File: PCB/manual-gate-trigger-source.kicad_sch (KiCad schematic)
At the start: 52 parts

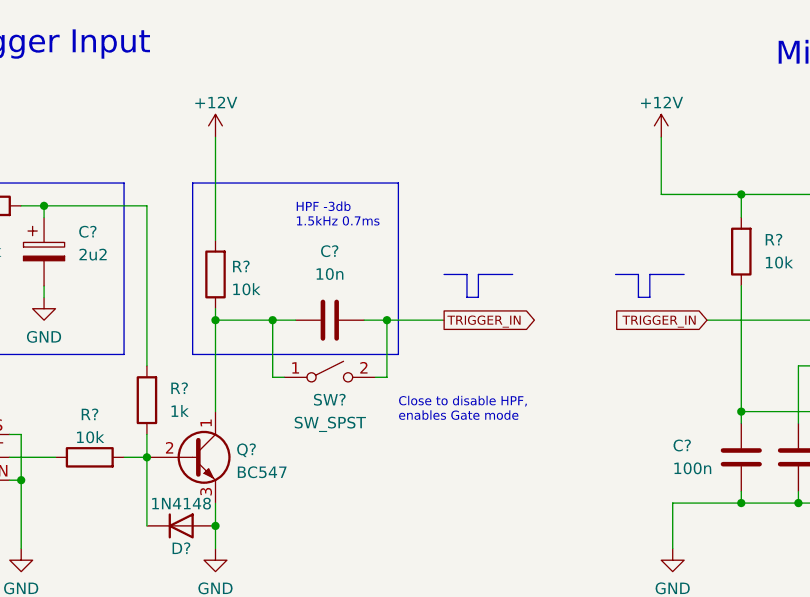
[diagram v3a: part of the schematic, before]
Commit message: :pencil2: Fix HPF for 555 input
As the signal is one-sided to V+, a second resistor was necessary.
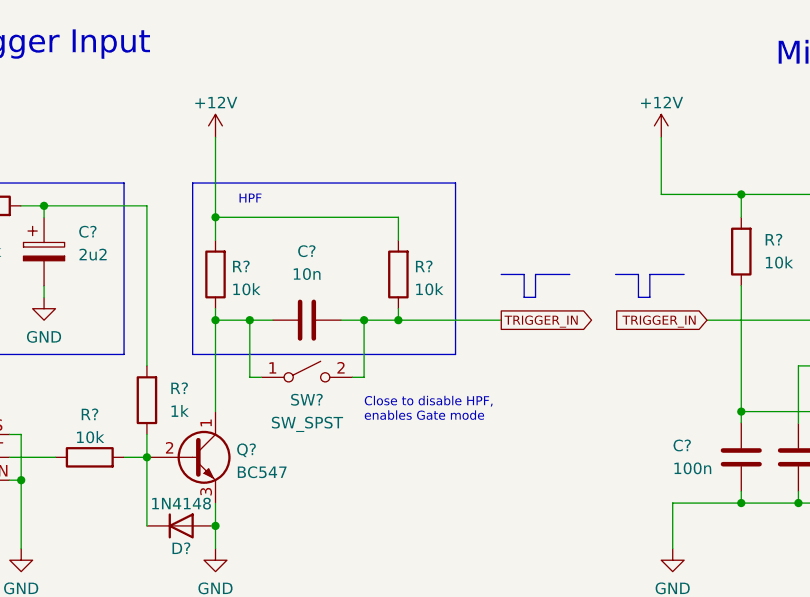
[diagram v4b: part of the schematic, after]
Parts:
- added R?: 10k, symbol Device:R
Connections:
- net +12V: now also R?.2
- net TRIGGER_IN: now also R?.1
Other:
- note added: "HPF"
- note removed: "HPF -3db 1.5kHz 0.7ms"
- moved on the sheet: C?, SW?
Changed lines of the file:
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@@
   (junction (at 102.87 157.48) (diameter 0) (color 0 0 0 0)
   )
-  (junction (at 80.01 58.42) (diameter 0) (color 0 0 0 0)
+  (junction (at 77.47 58.42) (diameter 0) (color 0 0 0 0)
   )
   (junction (at 198.12 138.43) (diameter 0) (color 0 0 0 0)
@@
   (junction (at 250.19 76.2) (diameter 0) (color 0 0 0 0)
   )
-  (junction (at 92.71 58.42) (diameter 0) (color 0 0 0 0)
+  (junction (at 93.98 58.42) (diameter 0) (color 0 0 0 0)
+  )
+  (junction (at 90.17 58.42) (diameter 0) (color 0 0 0 0)
   )
   (junction (at 73.66 81.28) (diameter 0) (color 0 0 0 0)
@@
   )
   (junction (at 232.41 130.81) (diameter 0) (color 0 0 0 0)
+  )
+  (junction (at 73.66 46.99) (diameter 0) (color 0 0 0 0)
   )
   (junction (at 247.65 146.05) (diameter 0) (color 0 0 0 0)
@@
   (no_connect (at 264.16 81.28))
   (no_connect (at 264.16 71.12))
-  (polyline (pts (xy 102.87 55.88) (xy 102.87 53.34))
+  (polyline (pts (xy 109.22 55.88) (xy 109.22 53.34))
     (stroke (width 0) (type solid) (color 0 0 0 0))
   )
@@
     (stroke (width 0) (type default) (color 0 0 0 0))
   )
-  (polyline (pts (xy 101.6 55.88) (xy 102.87 55.88))
+  (polyline (pts (xy 107.95 55.88) (xy 109.22 55.88))
     (stroke (width 0) (type solid) (color 0 0 0 0))
   )
@@
     (stroke (width 0) (type solid) (color 0 0 0 0))
   )
-  (wire (pts (xy 90.17 58.42) (xy 92.71 58.42))
+  (wire (pts (xy 87.63 58.42) (xy 90.17 58.42))
     (stroke (width 0) (type default) (color 0 0 0 0))
   )
@@
   )
   (wire (pts (xy 262.89 68.58) (xy 262.89 78.74))
+    (stroke (width 0) (type default) (color 0 0 0 0))
+  )
+  (wire (pts (xy 93.98 49.53) (xy 93.98 46.99))
     (stroke (width 0) (type default) (color 0 0 0 0))
   )
@@
     (stroke (width 0) (type solid) (color 0 0 0 0))
   )
-  (wire (pts (xy 92.71 58.42) (xy 92.71 64.77))
+  (wire (pts (xy 90.17 58.42) (xy 90.17 64.77))
     (stroke (width 0) (type default) (color 0 0 0 0))
   )
@@
   )
   (wire (pts (xy 153.67 78.74) (xy 190.5 78.74))
+    (stroke (width 0) (type default) (color 0 0 0 0))
+  )
+  (wire (pts (xy 93.98 46.99) (xy 73.66 46.99))
     (stroke (width 0) (type default) (color 0 0 0 0))
   )
@@
     (stroke (width 0) (type solid) (color 0 0 0 0))
   )
-  (polyline (pts (xy 71.12 43.18) (xy 93.98 43.18))
+  (polyline (pts (xy 71.12 43.18) (xy 100.33 43.18))
     (stroke (width 0) (type default) (color 0 0 0 0))
   )
@@
     (stroke (width 0) (type default) (color 0 0 0 0))
   )
-  (wire (pts (xy 73.66 58.42) (xy 80.01 58.42))
-    (stroke (width 0) (type default) (color 0 0 0 0))
-  )
-  (wire (pts (xy 91.44 64.77) (xy 92.71 64.77))
+  (wire (pts (xy 73.66 58.42) (xy 77.47 58.42))
+    (stroke (width 0) (type default) (color 0 0 0 0))
+  )
+  (wire (pts (xy 88.9 64.77) (xy 90.17 64.77))
     (stroke (width 0) (type default) (color 0 0 0 0))
   )
@@
     (stroke (width 0) (type default) (color 0 0 0 0))
   )
-  (wire (pts (xy 81.28 64.77) (xy 80.01 64.77))
+  (wire (pts (xy 78.74 64.77) (xy 77.47 64.77))
     (stroke (width 0) (type default) (color 0 0 0 0))
   )
@@
     (stroke (width 0) (type default) (color 0 0 0 0))
   )
+  (wire (pts (xy 73.66 46.99) (xy 73.66 49.53))
+    (stroke (width 0) (type default) (color 0 0 0 0))
+  )
   (wire (pts (xy 168.91 135.89) (xy 167.64 135.89))
     (stroke (width 0) (type default) (color 0 0 0 0))
@@
   )
   (wire (pts (xy 257.81 138.43) (xy 273.05 138.43))
+    (stroke (width 0) (type default) (color 0 0 0 0))
+  )
+  (wire (pts (xy 93.98 58.42) (xy 105.41 58.42))
     (stroke (width 0) (type default) (color 0 0 0 0))
   )
@@
     (stroke (width 0) (type default) (color 0 0 0 0))
   )
+  (wire (pts (xy 93.98 57.15) (xy 93.98 58.42))
+    (stroke (width 0) (type default) (color 0 0 0 0))
+  )
   (wire (pts (xy 170.18 68.58) (xy 170.18 63.5))
     (stroke (width 0) (type default) (color 0 0 0 0))
@@
     (stroke (width 0) (type default) (color 0 0 0 0))
   )
+  (wire (pts (xy 73.66 38.1) (xy 73.66 46.99))
+    (stroke (width 0) (type default) (color 0 0 0 0))
+  )
   (wire (pts (xy 247.65 146.05) (xy 257.81 146.05))
     (stroke (width 0) (type default) (color 0 0 0 0))
@@
     (stroke (width 0) (type default) (color 0 0 0 0))
   )
-  (polyline (pts (xy 101.6 53.34) (xy 101.6 55.88))
+  (polyline (pts (xy 107.95 53.34) (xy 107.95 55.88))
     (stroke (width 0) (type solid) (color 0 0 0 0))
   )
@@
     (stroke (width 0) (type default) (color 0 0 0 0))
   )
-  (polyline (pts (xy 93.98 43.18) (xy 93.98 62.23))
+  (polyline (pts (xy 100.33 43.18) (xy 100.33 62.23))
     (stroke (width 0) (type default) (color 0 0 0 0))
   )
@@
     (stroke (width 0) (type default) (color 0 0 0 0))
   )
-  (wire (pts (xy 92.71 58.42) (xy 99.06 58.42))
-    (stroke (width 0) (type default) (color 0 0 0 0))
-  )
-  (wire (pts (xy 80.01 58.42) (xy 80.01 64.77))
+  (wire (pts (xy 90.17 58.42) (xy 93.98 58.42))
+    (stroke (width 0) (type default) (color 0 0 0 0))
+  )
+  (wire (pts (xy 77.47 58.42) (xy 77.47 64.77))
     (stroke (width 0) (type default) (color 0 0 0 0))
   )
@@
     (stroke (width 0) (type default) (color 0 0 0 0))
   )
-  (polyline (pts (xy 93.98 62.23) (xy 71.12 62.23))
+  (polyline (pts (xy 100.33 62.23) (xy 71.12 62.23))
     (stroke (width 0) (type default) (color 0 0 0 0))
   )
@@
     (stroke (width 0) (type default) (color 0 0 0 0))
   )
-  (wire (pts (xy 73.66 38.1) (xy 73.66 49.53))
-    (stroke (width 0) (type default) (color 0 0 0 0))
-  )
   (polyline (pts (xy 64.77 144.78) (xy 82.55 144.78))
     (stroke (width 0) (type default) (color 0 0 0 0))
@@
     (stroke (width 0) (type default) (color 0 0 0 0))
   )
-  (polyline (pts (xy 102.87 53.34) (xy 106.68 53.34))
+  (polyline (pts (xy 109.22 53.34) (xy 113.03 53.34))
     (stroke (width 0) (type solid) (color 0 0 0 0))
   )
@@
     (stroke (width 0) (type default) (color 0 0 0 0))
   )
-  (wire (pts (xy 80.01 58.42) (xy 82.55 58.42))
+  (wire (pts (xy 77.47 58.42) (xy 80.01 58.42))
     (stroke (width 0) (type default) (color 0 0 0 0))
   )
@@
     (stroke (width 0) (type default) (color 0 0 0 0))
   )
-  (polyline (pts (xy 99.06 53.34) (xy 101.6 53.34))
+  (polyline (pts (xy 105.41 53.34) (xy 107.95 53.34))
     (stroke (width 0) (type solid) (color 0 0 0 0))
   )
@@
     (effects (font (size 1 1)) (justify left bottom))
   )
-  (text "Close to disable HPF,\nenables Gate mode" (at 93.98 69.85 0)
+  (text "Close to disable HPF,\nenables Gate mode" (at 90.17 69.85 0)
     (effects (font (size 1 1)) (justify left bottom))
   )
@@
     (effects (font (size 1 1)) (justify left bottom))
   )
-  (text "HPF -3db\n1.5kHz 0.7ms " (at 82.55 48.26 0)
+  (text "HPF" (at 76.2 45.72 0)
     (effects (font (size 1 1)) (justify left bottom))
   )
@@
     (effects (font (size 2.54 2.54)) (justify left bottom))
   )
-  (global_label "TRIGGER_IN" (shape output) (at 99.06 58.42 0) (fields_autoplaced)
+  (global_label "TRIGGER_IN" (shape output) (at 105.41 58.42 0) (fields_autoplaced)
     (effects (font (size 1 1)) (justify left))
-    (property "Intersheet References" "${INTERSHEET_REFS}" (id 0) (at 109.3886 58.3575 0)
+    (property "Intersheet References" "${INTERSHEET_REFS}" (id 0) (at 115.7386 58.3575 0)
       (effects (font (size 1 1)) (justify left) hide)
     )
@@
     (pin "2")
   )
-  (symbol (lib_id "Switch:SW_SPST") (at 86.36 64.77 0) (unit 1)
-    (in_bom yes) (on_board yes)
-    (property "Reference" "SW?" (id 0) (at 86.36 67.31 0))
-    (property "Value" "SW_SPST" (id 1) (at 86.36 69.85 0))
-    (property "Footprint" "" (id 2) (at 86.36 64.77 0)
-      (effects (font (size 1.27 1.27)) hide)
-    )
-    (property "Datasheet" "~" (id 3) (at 86.36 64.77 0)
+  (symbol (lib_id "Switch:SW_SPST") (at 83.82 64.77 0) (unit 1)
+    (in_bom yes) (on_board yes)
+    (property "Reference" "SW?" (id 0) (at 83.82 67.31 0))
+    (property "Value" "SW_SPST" (id 1) (at 83.82 69.85 0))
+    (property "Footprint" "" (id 2) (at 83.82 64.77 0)
+      (effects (font (size 1.27 1.27)) hide)
+    )
+    (property "Datasheet" "~" (id 3) (at 83.82 64.77 0)
       (effects (font (size 1.27 1.27)) hide)
     )
@@
     (pin "2")
   )
+  (symbol (lib_id "Device:R") (at 93.98 53.34 180) (unit 1)
+    (in_bom yes) (on_board yes) (fields_autoplaced)
+    (property "Reference" "R?" (id 0) (at 95.758 52.5053 0)
+      (effects (font (size 1.27 1.27)) (justify right))
+    )
+    (property "Value" "10k" (id 1) (at 95.758 55.0422 0)
+      (effects (font (size 1.27 1.27)) (justify right))
+    )
+    (property "Footprint" "" (id 2) (at 95.758 53.34 90)
+      (effects (font (size 1.27 1.27)) hide)
+    )
+    (property "Datasheet" "~" (id 3) (at 93.98 53.34 0)
+      (effects (font (size 1.27 1.27)) hide)
+    )
+    (pin "1")
+    (pin "2")
+  )
   (symbol (lib_id "power:Vdrive") (at 107.95 151.13 270) (unit 1)
     (in_bom yes) (on_board yes) (fields_autoplaced)
@@
     (pin "1")
   )
-  (symbol (lib_id "Device:C") (at 86.36 58.42 90) (unit 1)
-    (in_bom yes) (on_board yes) (fields_autoplaced)
-    (property "Reference" "C?" (id 0) (at 86.36 50.8 90))
-    (property "Value" "10n" (id 1) (at 86.36 53.34 90))
-    (property "Footprint" "" (id 2) (at 90.17 57.4548 0)
-      (effects (font (size 1.27 1.27)) hide)
-    )
-    (property "Datasheet" "~" (id 3) (at 86.36 58.42 0)
+  (symbol (lib_id "Device:C") (at 83.82 58.42 90) (unit 1)
+    (in_bom yes) (on_board yes) (fields_autoplaced)
+    (property "Reference" "C?" (id 0) (at 83.82 50.8 90))
+    (property "Value" "10n" (id 1) (at 83.82 53.34 90))
+    (property "Footprint" "" (id 2) (at 87.63 57.4548 0)
+      (effects (font (size 1.27 1.27)) hide)
+    )
+    (property "Datasheet" "~" (id 3) (at 83.82 58.42 0)
       (effects (font (size 1.27 1.27)) hide)
     )
@@
       (reference "R?") (unit 1) (value "10k") (footprint "")
     )
+    (path "/f08fae6e-44b8-4c56-be63-e88406367585"
+      (reference "R?") (unit 1) (value "10k") (footprint "")
+    )

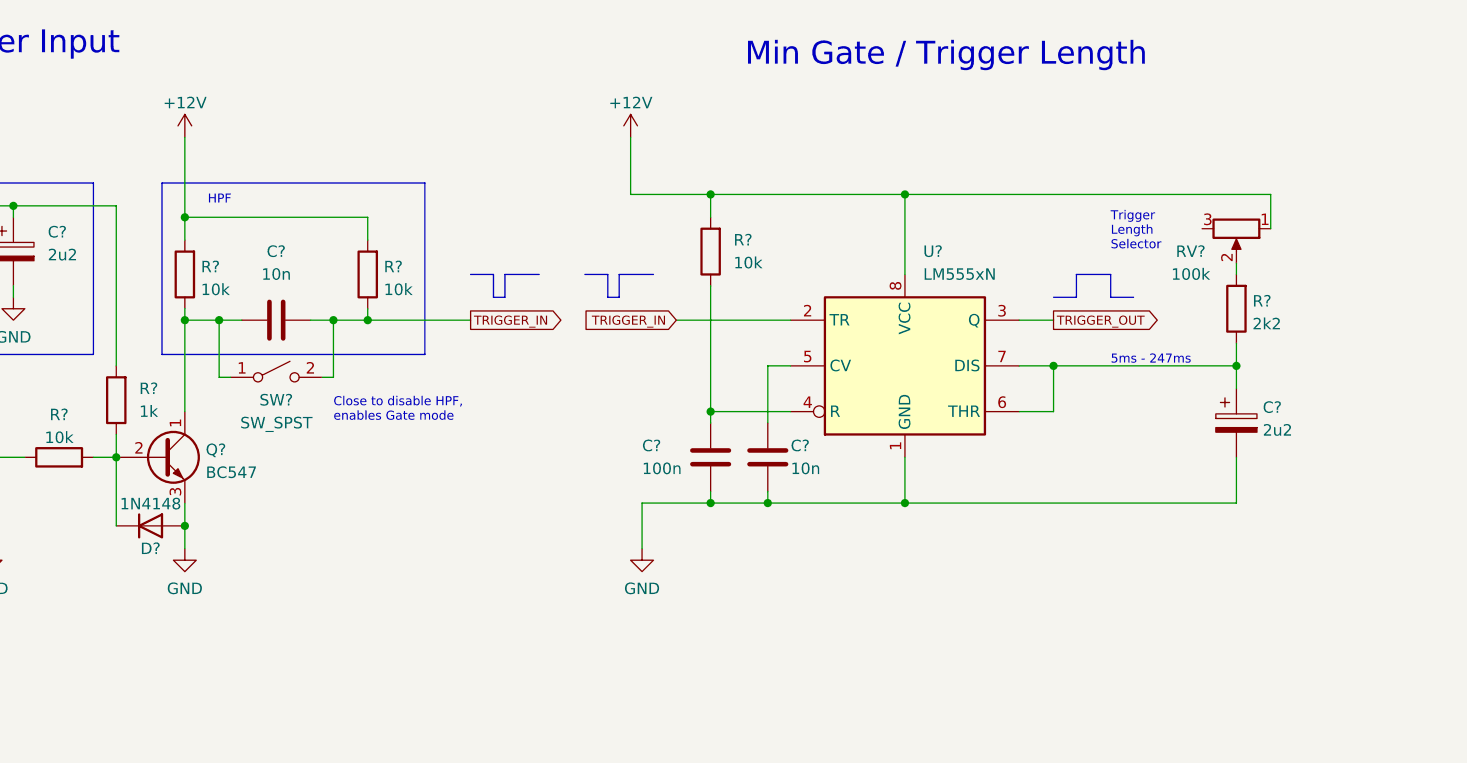
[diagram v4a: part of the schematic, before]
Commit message: :hammer: Move gate/trigger selector to 555 section
This is very specific to the 555 circuit, so it's better displayed
there.
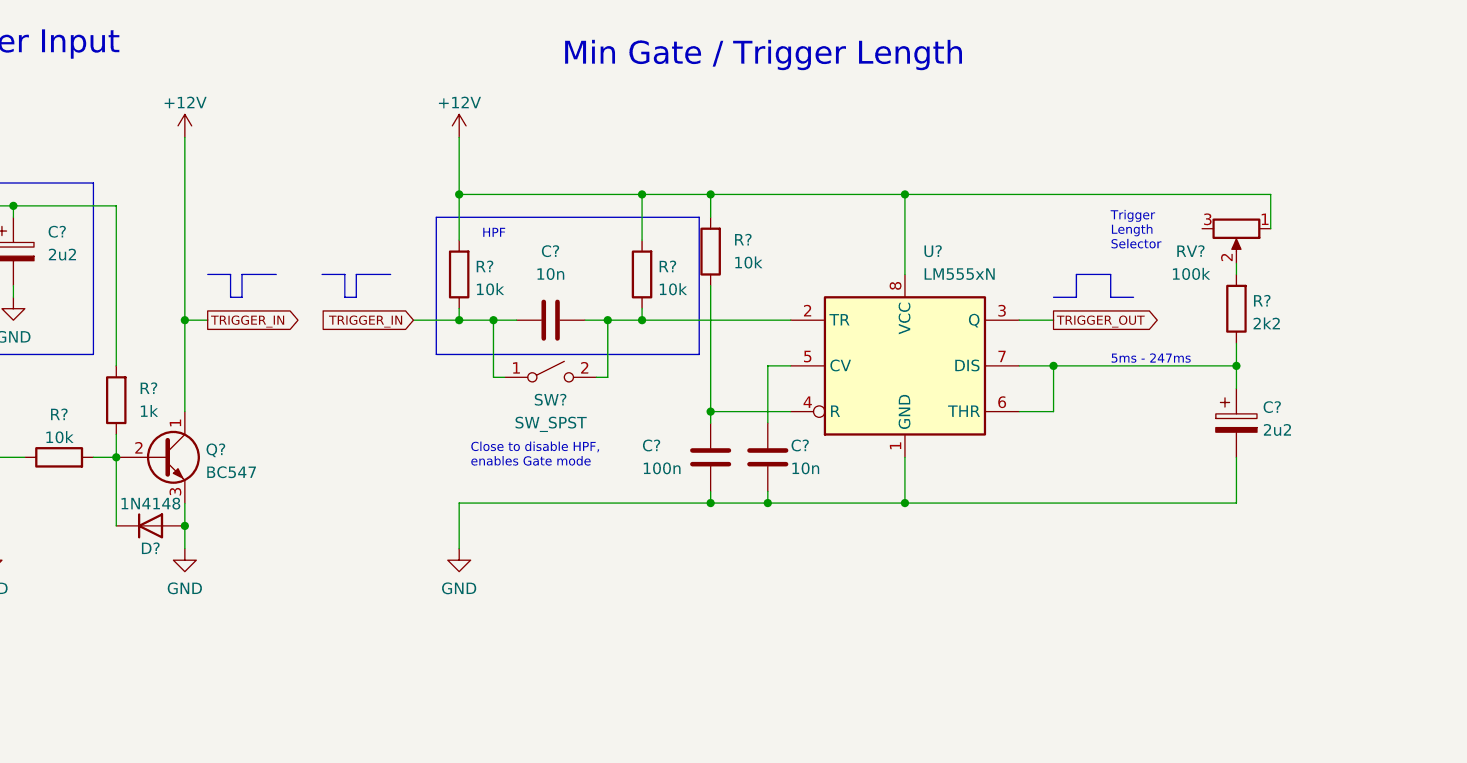
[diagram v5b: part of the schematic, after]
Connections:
- net +12V: now also C?.1, Q?.1 (C), R?.1, SW?.1 (A)
- net TRIGGER_IN: no longer names the net of C?.2, R?.1, SW?.2 (B), U?.2 (TR)
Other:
- moved on the sheet: C?, R?, SW?
